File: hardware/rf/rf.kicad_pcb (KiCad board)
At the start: 4 copper layers, 31.8 x 25.4 mm, 52 parts, among them J1 BGT24_Module_Castellations, J2 SMP, J3 SMP, J4 SMP, U1 ECS-2520S33-400, U2 LMX2491, U3 BGT24MTR12

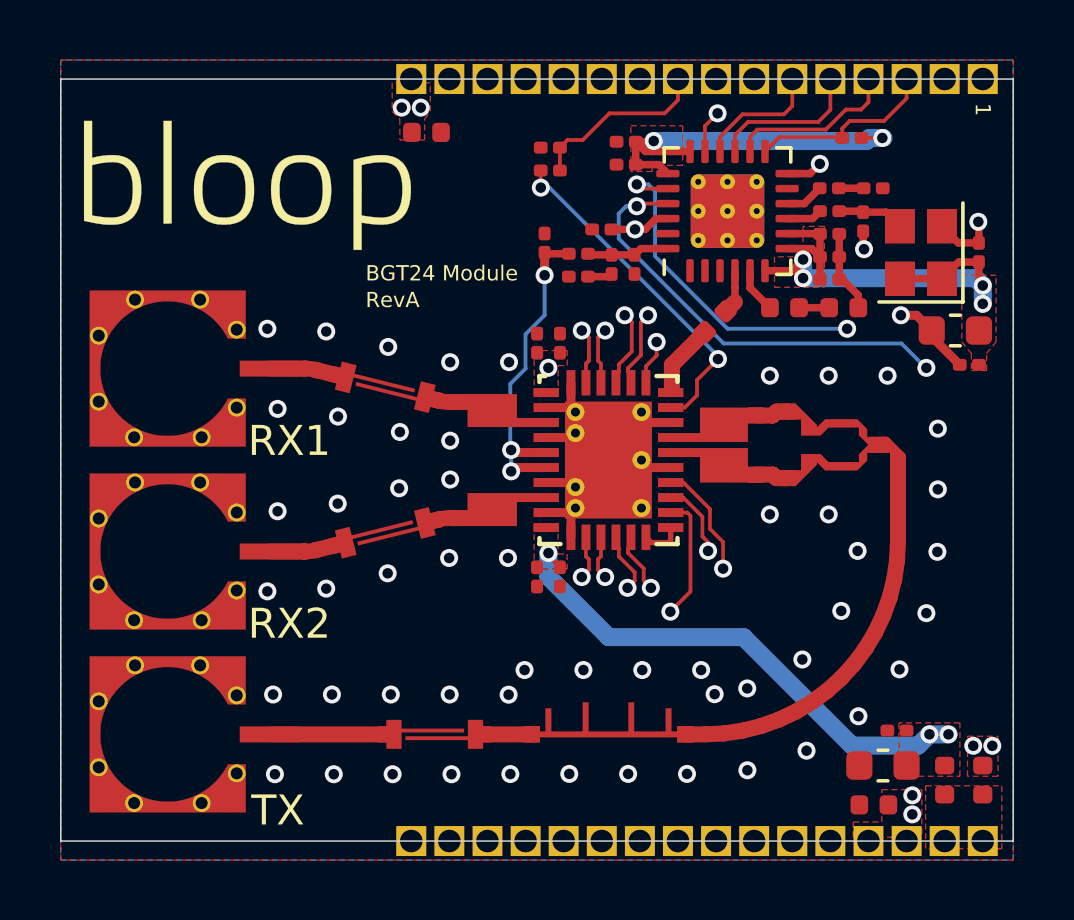
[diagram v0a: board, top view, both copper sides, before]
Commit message: Layout review edits with Austin. Added BGT24 Module FAB files and started the panel for the module
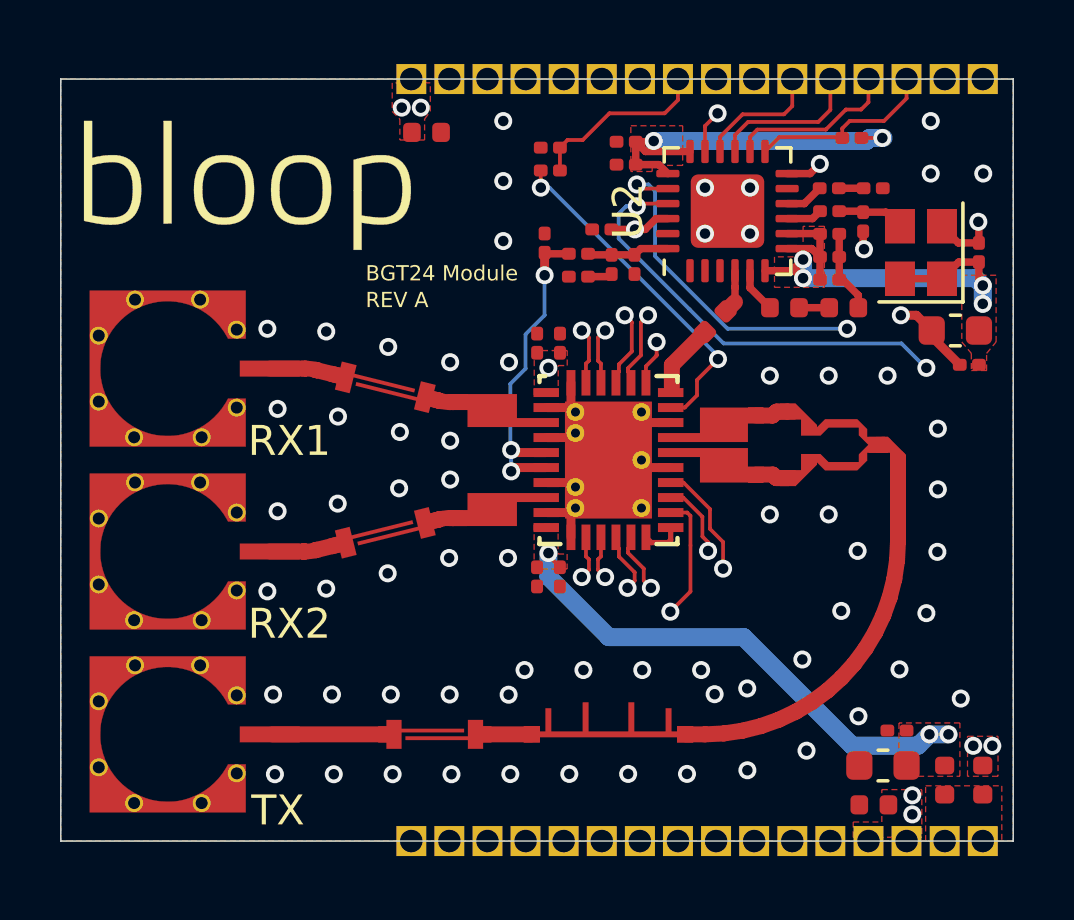
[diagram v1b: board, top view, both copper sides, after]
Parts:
- U2: footprint Package_DFN_QFN:VQFN-24-1EP_4x4mm_P0.5mm_EP2.45x2.45mm_ThermalVias -> Package_DFN_QFN:VQFN-24-1EP_4x4mm_P0.5mm_EP2.45x2.45mm
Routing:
- net GNDRF: vias 53 -> 64
- added copper zone on In2.Cu, net GNDRF
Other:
- board text added: "REV A"
- board text removed: "1"
- board text removed: "RevA"

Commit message: Updated panel with updated module layout
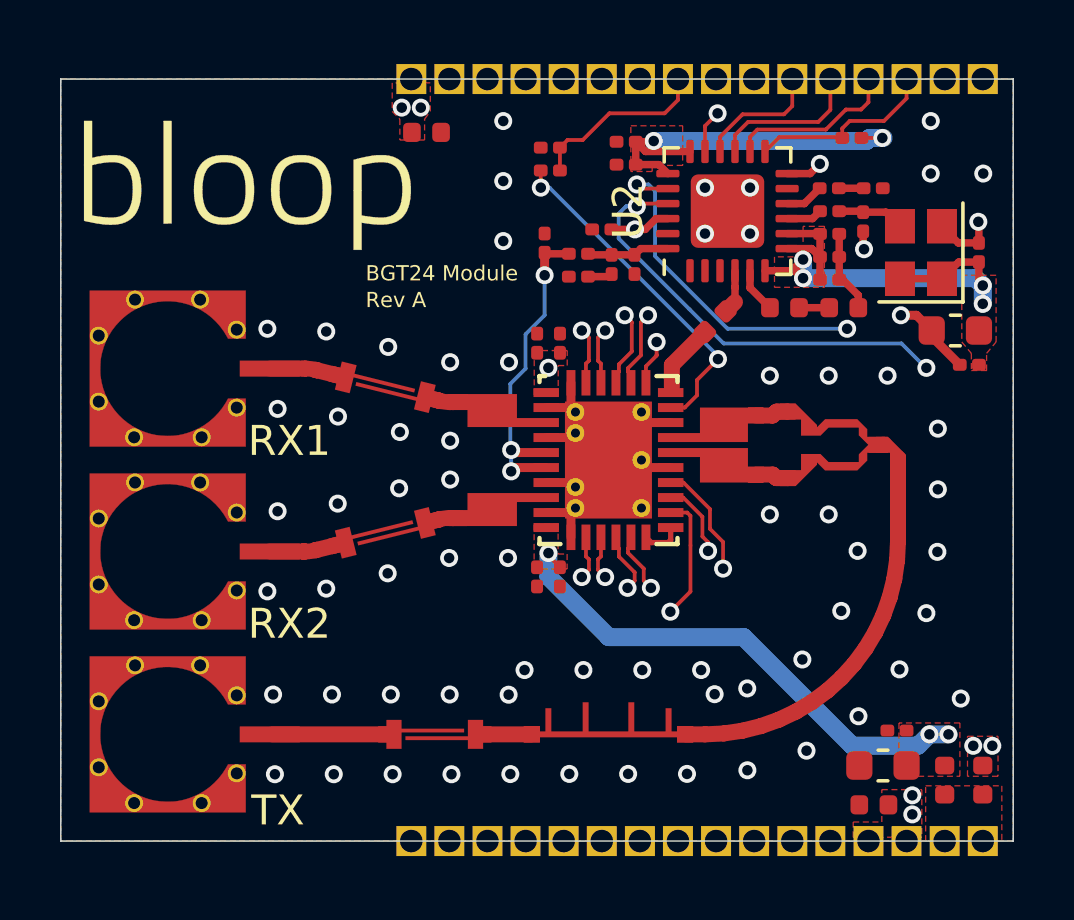
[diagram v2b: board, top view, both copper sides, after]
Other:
- board text added: "Rev A"
- board text removed: "REV A"
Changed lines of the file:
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@@
     (effects (font (size 1 1) (thickness 0.15)))
   )
-  (gr_text "REV A" (at 145.542 89.5779) (layer F.SilkS)
+  (gr_text "Rev A" (at 145.542 89.5779) (layer F.SilkS)
     (effects (font (size 0.508 0.508) (thickness 0.0762)) (justify left))
   )

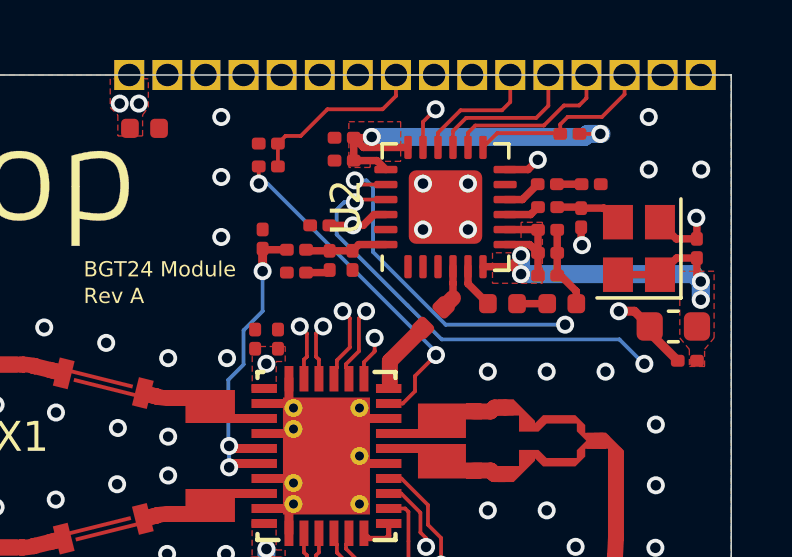
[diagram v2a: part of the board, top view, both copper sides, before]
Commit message: Assigned MPNs to components and generated BOM. Small layout edits for changed part footprints
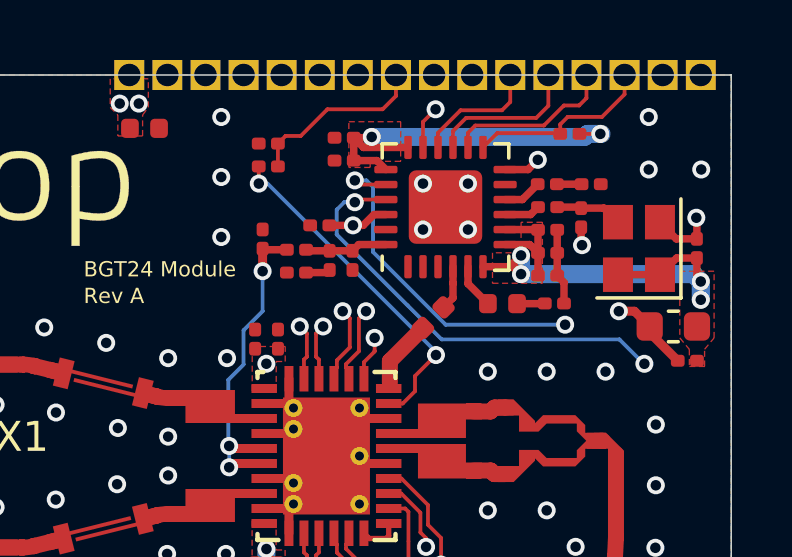
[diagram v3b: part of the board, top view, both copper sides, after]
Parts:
- ?: renamed from ~; value LOGO -> (none)
- C7, C8: value 0.1u -> 100n
- R1, R2, R3, R5, R6, R7: footprint Capacitor_SMD:C_0201_0603Metric -> Resistor_SMD:R_0201_0603Metric
- R4: footprint Capacitor_SMD:C_0402_1005Metric -> Resistor_SMD:R_0201_0603Metric
- moved R4 0.25 mm to (161.2, 89.8)

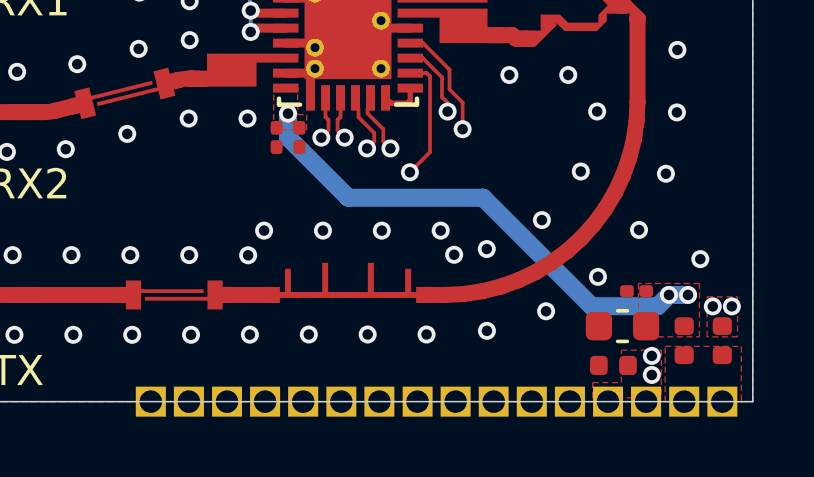
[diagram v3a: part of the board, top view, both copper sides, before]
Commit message: Added basic 3d model for BGT24 Module footprint. Final edits to layout and panel layout. Updated FAB files for each.
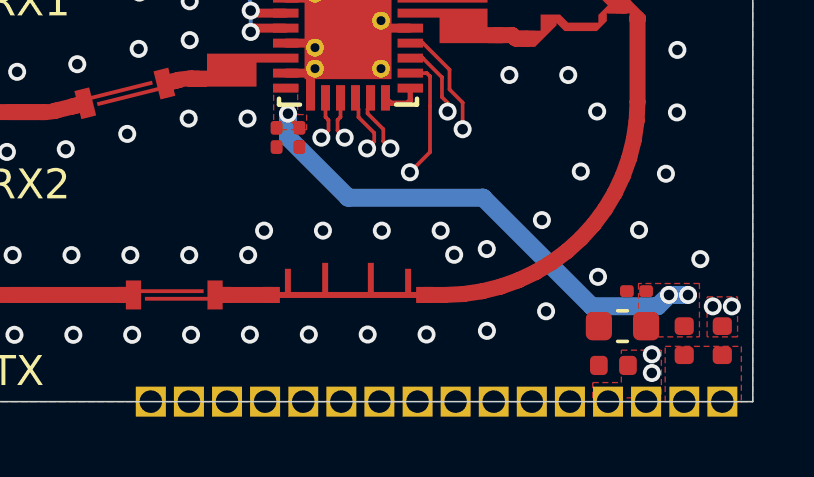
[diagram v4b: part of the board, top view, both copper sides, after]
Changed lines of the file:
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@@
-(kicad_pcb (version 20171130) (host pcbnew 5.1.4)
+(kicad_pcb (version 20171130) (host pcbnew "(5.1.4)-1")
   (general
     (thickness 1.06)
-    (drawings 39)
+    (drawings 43)
     (tracks 535)
     (zones 0)
@@
     (32 B.Adhes user)
     (33 F.Adhes user)
-    (34 B.Paste user hide)
-    (35 F.Paste user hide)
+    (34 B.Paste user)
+    (35 F.Paste user)
     (36 B.SilkS user)
     (37 F.SilkS user)
@@
     )
   )
+  (dimension 25.4 (width 0.15) (layer Dwgs.User)
+    (gr_text "25.400 mm" (at 128.24 94.9119 90) (layer Dwgs.User)
+      (effects (font (size 1 1) (thickness 0.15)))
+    )
+    (feature1 (pts (xy 135.382 82.2119) (xy 128.953579 82.2119)))
+    (feature2 (pts (xy 135.382 107.6119) (xy 128.953579 107.6119)))
+    (crossbar (pts (xy 129.54 107.6119) (xy 129.54 82.2119)))
+    (arrow1a (pts (xy 129.54 82.2119) (xy 130.126421 83.338404)))
+    (arrow1b (pts (xy 129.54 82.2119) (xy 128.953579 83.338404)))
+    (arrow2a (pts (xy 129.54 107.6119) (xy 130.126421 106.485396)))
+    (arrow2b (pts (xy 129.54 107.6119) (xy 128.953579 106.485396)))
+  )
+  (dimension 25.4 (width 0.15) (layer Dwgs.User)
+    (gr_text "1.0000 in" (at 131.034 94.9119 90) (layer Dwgs.User)
+      (effects (font (size 1 1) (thickness 0.15)))
+    )
+    (feature1 (pts (xy 135.382 82.2119) (xy 131.747579 82.2119)))
+    (feature2 (pts (xy 135.382 107.6119) (xy 131.747579 107.6119)))
+    (crossbar (pts (xy 132.334 107.6119) (xy 132.334 82.2119)))
+    (arrow1a (pts (xy 132.334 82.2119) (xy 132.920421 83.338404)))
+    (arrow1b (pts (xy 132.334 82.2119) (xy 131.747579 83.338404)))
+    (arrow2a (pts (xy 132.334 107.6119) (xy 132.920421 106.485396)))
+    (arrow2b (pts (xy 132.334 107.6119) (xy 131.747579 106.485396)))
+  )
+  (dimension 31.75 (width 0.15) (layer Dwgs.User)
+    (gr_text "31.750 mm" (at 151.257 74.9) (layer Dwgs.User)
+      (effects (font (size 1 1) (thickness 0.15)))
+    )
+    (feature1 (pts (xy 167.132 82.2119) (xy 167.132 75.613579)))
+    (feature2 (pts (xy 135.382 82.2119) (xy 135.382 75.613579)))
+    (crossbar (pts (xy 135.382 76.2) (xy 167.132 76.2)))
+    (arrow1a (pts (xy 167.132 76.2) (xy 166.005496 76.786421)))
+    (arrow1b (pts (xy 167.132 76.2) (xy 166.005496 75.613579)))
+    (arrow2a (pts (xy 135.382 76.2) (xy 136.508504 76.786421)))
+    (arrow2b (pts (xy 135.382 76.2) (xy 136.508504 75.613579)))
+  )
+  (dimension 31.75 (width 0.15) (layer Dwgs.User)
+    (gr_text "1.2500 in" (at 151.257 77.44) (layer Dwgs.User)
+      (effects (font (size 1 1) (thickness 0.15)))
+    )
+    (feature1 (pts (xy 167.132 82.2119) (xy 167.132 78.153579)))
+    (feature2 (pts (xy 135.382 82.2119) (xy 135.382 78.153579)))
+    (crossbar (pts (xy 135.382 78.74) (xy 167.132 78.74)))
+    (arrow1a (pts (xy 167.132 78.74) (xy 166.005496 79.326421)))
+    (arrow1b (pts (xy 167.132 78.74) (xy 166.005496 78.153579)))
+    (arrow2a (pts (xy 135.382 78.74) (xy 136.508504 79.326421)))
+    (arrow2b (pts (xy 135.382 78.74) (xy 136.508504 78.153579)))
+  )
   (gr_circle (center 166.116 83.4069) (end 166.116 83.4069) (layer F.SilkS) (width 0.5))
   (gr_line (start 161.830066 101.704174) (end 161.406148 102.171896) (layer F.Mask) (width 3.3174))
@@
   (via (at 144.614908 96.363926) (size 0.6) (drill 0.35) (layers F.Cu B.Cu) (net 1))
   (via (at 148.362418 95.5615) (size 0.6) (drill 0.35) (layers F.Cu B.Cu) (net 1))
-  (via (at 150.310981 102.733459) (size 0.6) (drill 0.35) (layers F.Cu B.Cu) (net 1))
+  (via (at 150.310981 102.72522) (size 0.6) (drill 0.35) (layers F.Cu B.Cu) (net 1))
   (via (at 158.270012 105.2522) (size 0.6) (drill 0.35) (layers F.Cu B.Cu) (net 1))
   (via (at 160.241658 104.599852) (size 0.6) (drill 0.35) (layers F.Cu B.Cu) (net 1))
@@
   (via (at 165.9678 86.9696) (size 0.6) (drill 0.35) (layers F.Cu B.Cu) (net 2))
   (segment (start 165.98654 86.98834) (end 165.9678 86.9696) (width 0.25) (layer F.Cu) (net 2))
-  (via (at 163.7665 106.0879) (size 0.6) (drill 0.35) (layers F.Cu B.Cu) (net 2))
-  (via (at 163.7665 106.7229) (size 0.6) (drill 0.35) (layers F.Cu B.Cu) (net 2))
+  (via (at 163.7665 106.65714) (size 0.6) (drill 0.35) (layers F.Cu B.Cu) (net 2))
   (via (at 163.3855 90.0859) (size 0.6) (drill 0.35) (layers F.Cu B.Cu) (net 2))
   (segment (start 163.906 90.0859) (end 164.414 90.5939) (width 0.3) (layer F.Cu) (net 2))
@@
   (segment (start 164.414 90.8019) (end 165.349 91.7369) (width 0.3) (layer F.Cu) (net 2))
   (segment (start 164.414 90.5939) (end 164.414 90.8019) (width 0.3) (layer F.Cu) (net 2))
+  (via (at 163.7665 106.03738) (size 0.6) (drill 0.35) (layers F.Cu B.Cu) (net 2))
   (segment (start 160.168 86.364) (end 160.68 85.852) (width 0.25) (layer F.Cu) (net 3))
   (segment (start 159.5945 86.364) (end 160.168 86.364) (width 0.25) (layer F.Cu) (net 3))
@@
         (xy 162.258427 97.466896) (xy 162.244299 97.966896) (xy 162.168427 98.536896) (xy 162.068427 99.036896) (xy 161.878427 99.586896)
         (xy 161.668427 100.076896) (xy 161.378427 100.586896) (xy 161.068427 101.006896) (xy 160.678427 101.416896) (xy 160.293128 101.796896)
-        (xy 159.873128 102.097214) (xy 159.363128 102.407214) (xy 158.868427 102.626896) (xy 158.344869 102.814426) (xy 157.803427 102.936896)
-        (xy 157.477981 103.006896) (xy 156.877981 103.0272)
+        (xy 159.873128 102.097214) (xy 159.363128 102.407214) (xy 158.868427 102.626896) (xy 158.35376 102.814426) (xy 157.76448 102.96144)
+        (xy 157.2641 103.0224) (xy 156.877981 103.0272)
       )
     )

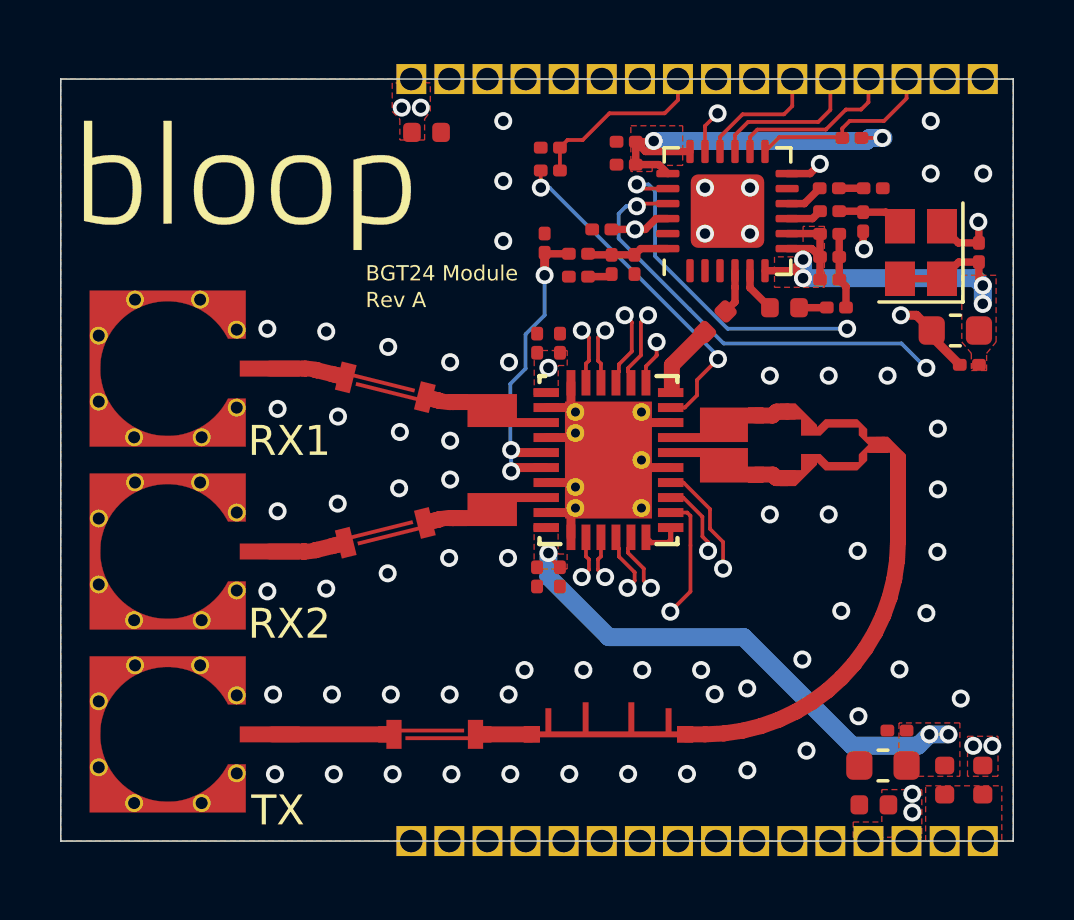
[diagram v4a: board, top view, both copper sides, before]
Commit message: Updated BGT24 Module layout and panel with new castellation footprint and adjusted some vias. Re-generated FAB outputs.
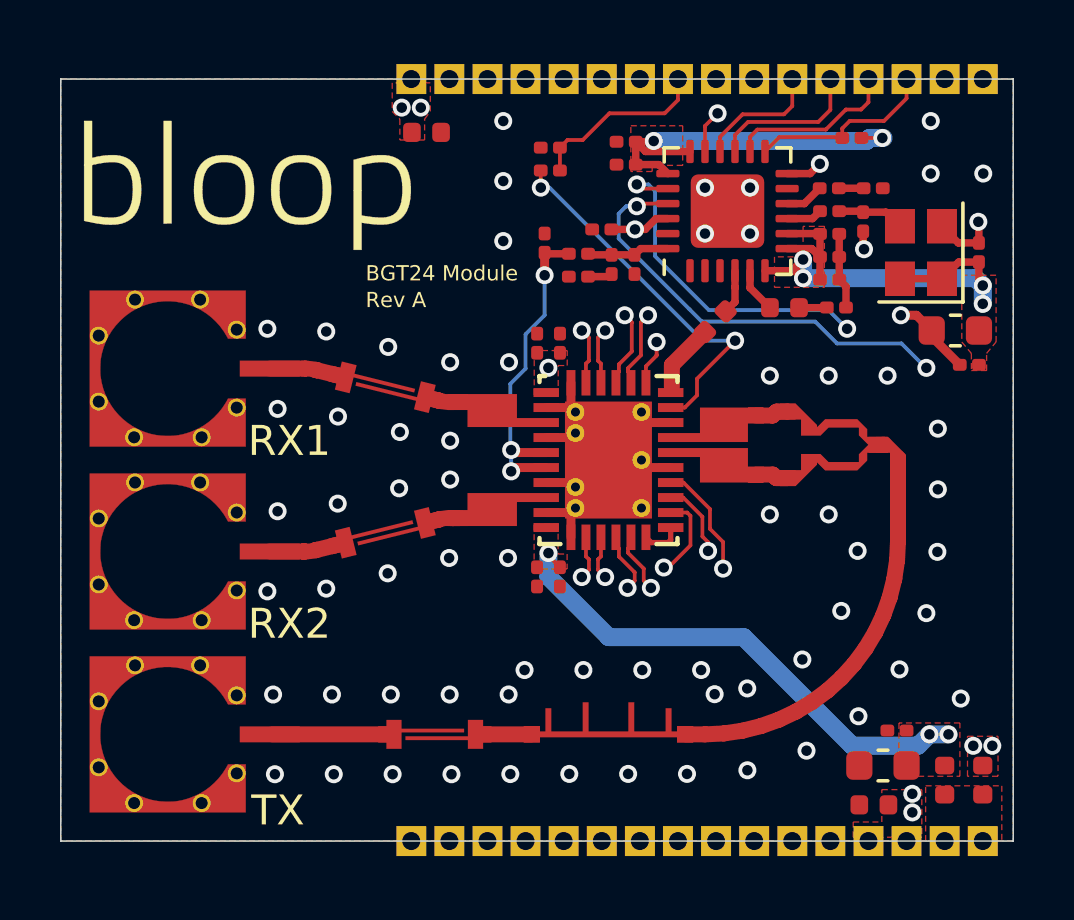
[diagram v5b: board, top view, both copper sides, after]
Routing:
- net Net-(R7-Pad2): track 11.4 -> 12.6 mm
